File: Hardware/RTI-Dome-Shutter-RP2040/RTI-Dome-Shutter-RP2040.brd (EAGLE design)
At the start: 111.1 x 76.3 mm, 107 parts, among them IC2 24LC64T-I/SN, IC3 FT232RL, IC4 RASPBERRY_PI_PICO, IC8 REG1117-3.3V, IC9 REG1117-5V, J2 XT60PW-M, U1 W5500, X13 PN61729-S, X9 J1011F21PNL

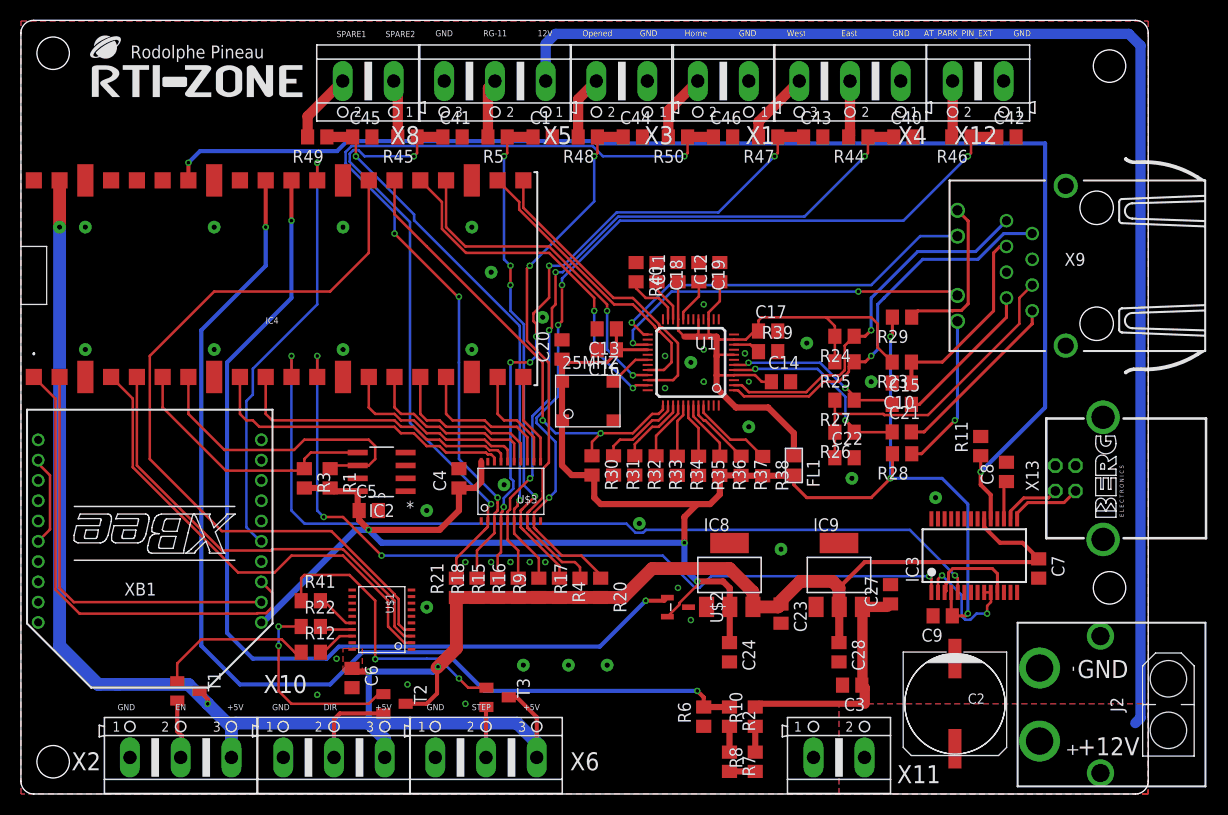
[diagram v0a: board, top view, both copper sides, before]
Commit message: New RP2040 shutter board
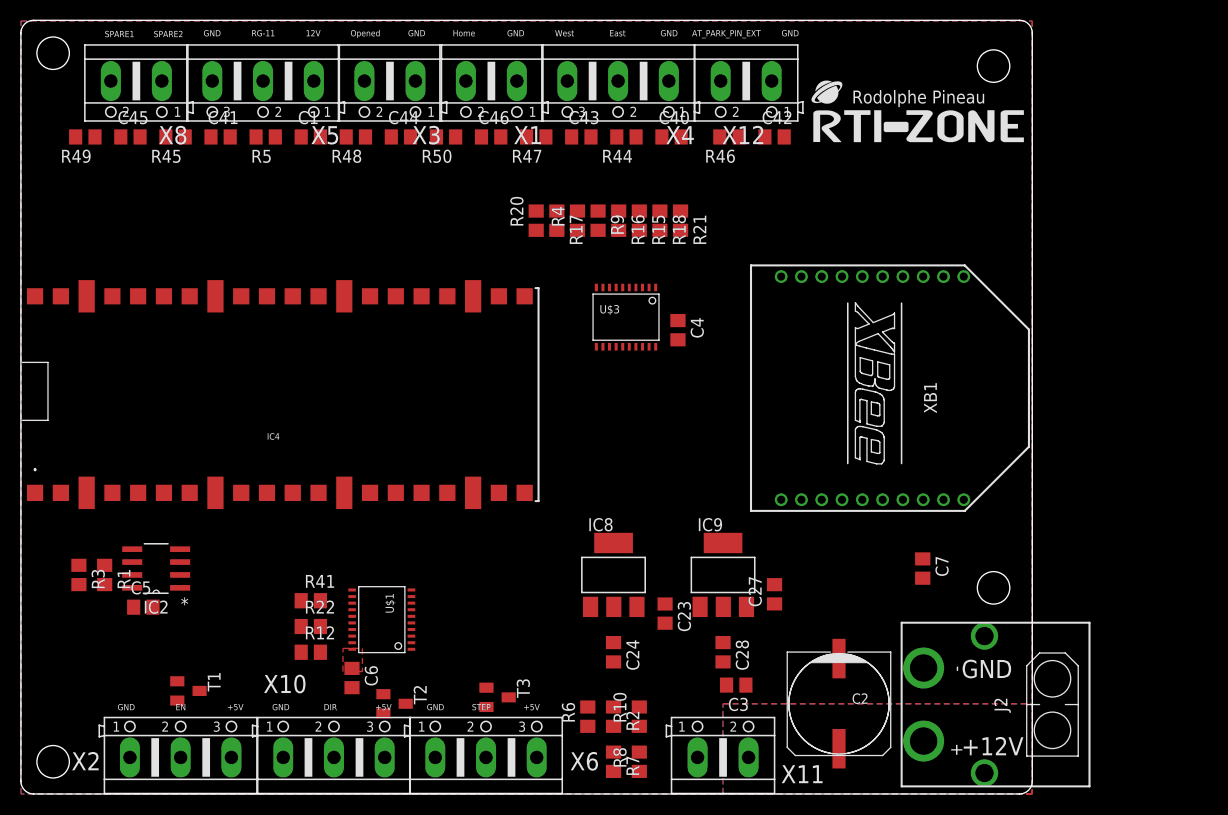
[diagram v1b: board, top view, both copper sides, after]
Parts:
- removed 25MHZ: CB3LV-OSCILATOR, rti:SMD-7050_4P
- removed C10: 22nF, rcl:C0805
- removed C11, C12, C14, C16, C17, C20, C8, C9: 100nF, rcl:C0805
- removed C13, C18, C22: 10nF, rcl:C0805
- removed C15, C21: 6.8nF, rcl:C0805
- removed C19: 4.7uF, rcl:C0805
- removed FL1: BLM21AG121SN1D, BLM21AG121SN1D:L0805
- removed IC3: FT232RL, ftdichip:SSOP28
- removed R11: 10K, rcl:R0805
- removed R23: 10 1%, rcl:R0805
- removed R24, R25, R26, R27: 49.9 1%, rcl:R0805
- removed R28, R29: 330, rcl:R0805
- removed R30, R31, R32, R33, R34, R35, R36, R37, R38, R40: 4.7K, rcl:R0805
- removed R39: 12.4K 1%, rcl:R0805
- removed U$2: MCP120T, MCP120T:SOT95P237X112-3N
- removed U1: W5500, W5500:LQFP48
- removed X13: PN61729-S, rti:PN61729-S
- removed X9: J1011F21PNL, rti:J1011F21PNL
- moved XB1 72.6 mm to (83.9, 40.0), turned to 270 degrees
- moved U$4 71.3 mm to (78.1, 64.3)
- moved R21 42.4 mm to (65.0, 56.5), turned to 270 degrees
- moved R18 40.4 mm to (63.0, 56.5), turned to 270 degrees
- moved R15 38.8 mm to (61.0, 56.5), turned to 270 degrees
- moved R16 37.5 mm to (58.9, 56.5), turned to 270 degrees
- moved R20 36.7 mm to (50.8, 56.5), turned to 90 degrees
- moved R9 36.7 mm to (56.9, 56.5), turned to 270 degrees
- moved R17 36.3 mm to (52.8, 56.5), turned to 270 degrees
- moved R4 36.2 mm to (54.9, 56.5), turned to 90 degrees
- moved C4 26.1 mm to (64.8, 45.7), turned to 270 degrees
- moved C5 24.2 mm to (12.1, 18.4)
- moved IC2 24.2 mm to (13.3, 22.2)
- moved R1 24.2 mm to (8.26, 21.6)
- moved R3 24.2 mm to (5.71, 21.6)
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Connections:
- removed net ACT_LED: U1.27, X9.11
- removed net AVDD: C11.1, C12.1, C14.1, C17.1, FL1.1, R23.2, R24.2, R25.2, U1.11, U1.15, U1.17, U1.21, U1.4, U1.8
- removed net DTR_DSR_DCD: IC3.10, IC3.2, IC3.9
- removed net INT_N: U1.36
- removed net LINK_ACK: U1.25, X9.10
- removed net N$10: R28.1, X9.12
- removed net N$11: C15.2, X9.7
- removed net N$12: C21.2, X9.8
- removed net N$13: C10.1, R23.1, X9.3
- removed net N$17: U1.26
- removed net N$22: R31.1, U1.38
- removed net N$23: R32.1, U1.39
- removed net N$24: R33.1, U1.40
- removed net N$25: R34.1, U1.41
- removed net N$26: R35.1, U1.42
- removed net N$27: R36.1, U1.43
- removed net N$28: R37.1, U1.44
- removed net N$29: R38.1, U1.45
- removed net N$31: C19.2, U1.20
- removed net N$32: U1.18
- removed net N$33: C18.2, U1.22
- removed net N$34: R39.1, U1.10
- removed net N$35: R40.2, U1.23
- removed net N$6: C8.1, IC3.17
- removed net N$7: C22.1, R26.2, R27.2, X9.6
- removed net N$8: R29.1, X9.9
- removed net RTS_CTS: IC3.11, IC3.3
- removed net RXN: C21.1, R26.1, U1.5
- removed net RXP: C15.1, R27.1, U1.6
- removed net TXN: R25.1, U1.1, X9.2
- removed net TXP: R24.1, U1.2, X9.1
- removed net USBD_N: IC3.16, X13.2
- removed net USBD_P: IC3.15, X13.3
- removed net USB_VCC: X13.1
- removed net XI: 25MHZ.3, U1.30
- removed net XO: U1.31
- net 3.3V: no longer 25MHZ.1, 25MHZ.4, C13.1, C16.1, C20.1, C9.1, FL1.2, IC3.4, R28.2, R29.2, R30.2, R36.2, R37.2, R38.2, U$2.2, U1.28
- net ETH_CS: no longer U1.32
- net ETH_RESET: no longer R30.1, U1.37
- net FTDI_RESET: no longer IC3.19, R11.1
- net GND: no longer 25MHZ.2, C10.2, C11.2, C12.2, C13.2, C14.2, C16.2, C17.2, C18.1, C19.1, C20.2, C22.2, C8.2, C9.2, IC3.18, IC3.21, IC3.25, IC3.7, R11.2, R31.2, R32.2, R33.2, R34.2, R35.2, R39.2, R40.1, U$2.3, U1.14, U1.16, U1.19, U1.29, U1.3, U1.48, U1.9, X13.4, X13.S1, X13.S2, X9.4, X9.5, X9.M1, X9.M2
- net RESET: no longer U$2.1
- net RX2: no longer IC3.1
- net SCLK: no longer U1.33
- net SDI: no longer U1.34
- net SDO: no longer U1.35
- net TX2: no longer IC3.5
- net VCC: no longer IC3.20
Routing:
- net VCC: track 219.2 -> 0.00 mm, vias 4 -> 0
- net 3.3V: track 197.7 -> 0.00 mm, vias 6 -> 0
- net +12V: track 154.1 -> 0.00 mm
- net FTDI_RESET: track 128.8 -> 0.00 mm, vias 2 -> 0
- net VPIN: track 106.3 -> 0.00 mm, vias 2 -> 0
- net RESET: track 94.2 -> 0.00 mm, vias 2 -> 0
- net HOME_SHUTTER_CLOSED_IN_5V: track 87.8 -> 0.00 mm, vias 4 -> 0
- net TX2: track 87.4 -> 0.00 mm, vias 2 -> 0
- net AT_PARK_PIN_IN_5V: track 86.0 -> 0.00 mm, vias 4 -> 0
- net RX2: track 82.9 -> 0.00 mm, vias 4 -> 0
- net M_STEP: track 77.4 -> 0.00 mm
- net BUTTON_EAST_OPEN_5V: track 72.4 -> 0.00 mm, vias 4 -> 0
- net AVDD: track 67.6 -> 0.00 mm
- net BUTTON_WEST_CLOSE_IN_5V: track 65.8 -> 0.00 mm, vias 6 -> 0
- net SPARE1_IN_5V: track 60.8 -> 0.00 mm, vias 2 -> 0
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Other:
- board size 111.1 x 76.3 mm -> 99.7 x 76.3 mm
- board text added: "Dome Shutter"
- board text removed: "Dome Rotator / RoR"

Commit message: Switching to 0603 for resistor and capacitors
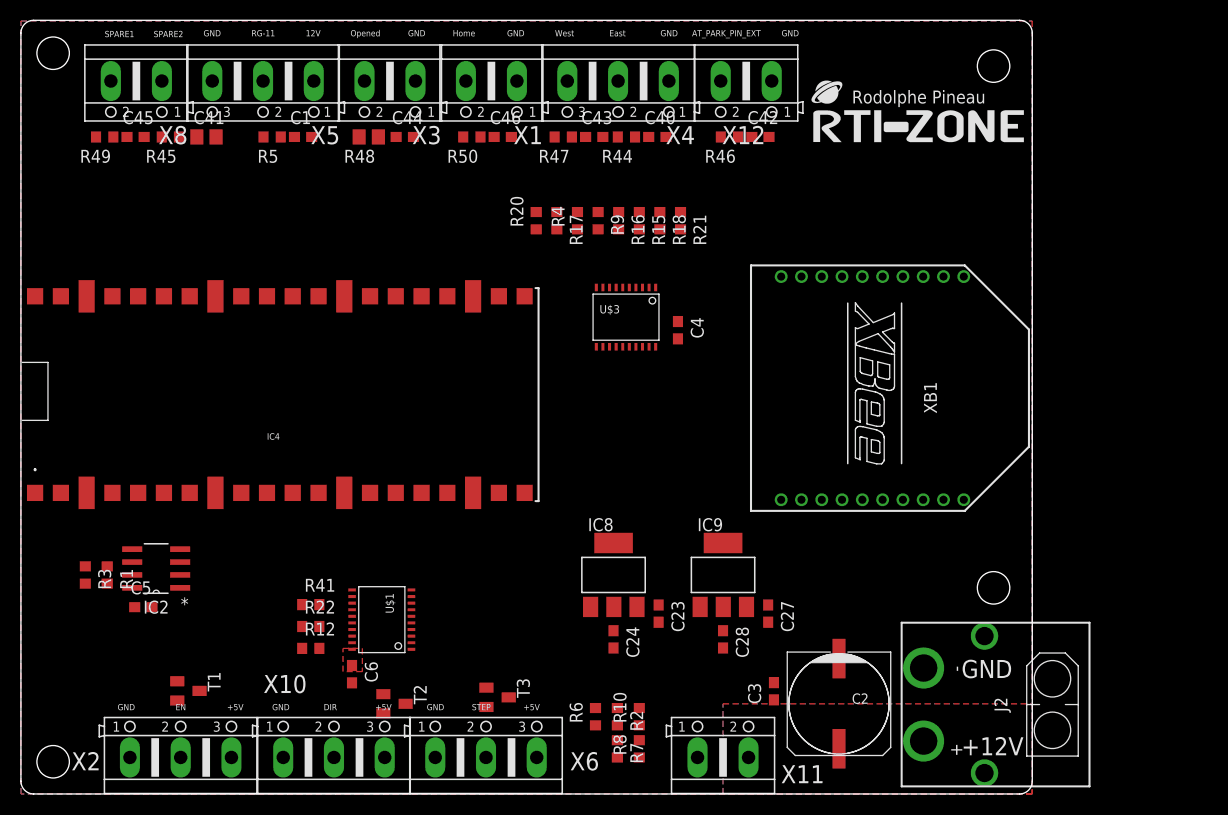
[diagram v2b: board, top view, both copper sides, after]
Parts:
- removed C7: 100nF, rcl:C0805
- C1, C23, C24, C27, C28, C3, C4, C40, C42, C43, C44, C45, C46, C5, C6: device rcl:C0805 -> rcl:C0603
- R1, R10, R12, R15, R16, R17, R18, R2, R20, R21, R22, R3, R4, R41, R44, R45, R46, R47, R49, R5, R50, R6, R7, R8, R9: device rcl:R0805 -> rcl:R0603
- moved C3 3.76 mm to (74.2, 10.1), turned to 90 degrees
- moved R47 2.67 mm to (53.5, 64.8)
- moved R50 2.54 mm to (44.5, 64.8)
- moved C27 2.01 mm to (73.7, 17.8), turned to 270 degrees
- moved R49 1.91 mm to (8.26, 64.8)
- moved C40 1.40 mm to (62.7, 64.8)
- moved C42 1.40 mm to (72.9, 64.8)
- moved C41 1.40 mm to (18.3, 64.8)
- moved R7 1.33 mm to (58.8, 4.45)
- moved C43 1.27 mm to (56.5, 64.8)
- moved R8 1.27 mm to (61.0, 4.45)
- moved C24 1.27 mm to (58.4, 15.2)
- moved C28 1.27 mm to (69.2, 15.2)
- moved R48 1.27 mm to (34.3, 64.8)
- moved C46 1.14 mm to (47.5, 64.8)
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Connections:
- net GND: no longer C7.2
- net VCC: no longer C7.1

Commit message: Routed RP2040 Shutter board
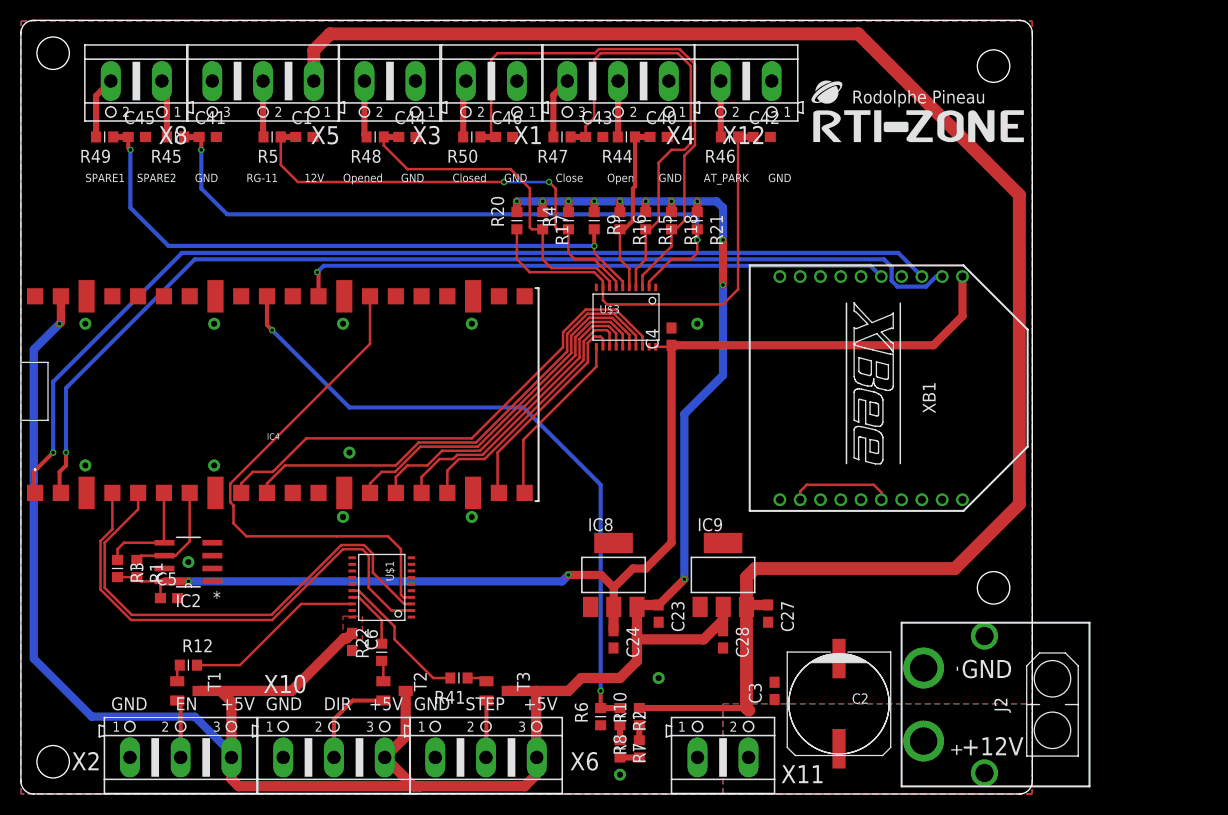
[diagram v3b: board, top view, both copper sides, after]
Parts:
- C1, C23, C24, C27, C28, C3, C4, C40, C42, C43, C44, C45, C46, C5, C6: device rcl:C0603 -> rti:C0603
- C41: device rcl:C0805 -> rti:C0603
- IC2: device Microchip_By_element14_Batch_1:SOIC127P600X175-8N -> rti:SOIC127P600X175-8N
- R1, R10, R12, R15, R16, R17, R18, R2, R20, R21, R22, R3, R4, R41, R44, R45, R46, R47, R49, R5, R50, R6, R7, R8, R9: device rcl:R0603 -> rti:R0603
- R48: device rcl:R0805 -> rti:R0603
- moved R41 16.3 mm to (43.2, 11.4), turned to 180 degrees
- moved R12 12.2 mm to (16.5, 12.7)
- moved R22 7.43 mm to (35.6, 14.0), turned to 90 degrees
- moved R3 3.24 mm to (9.53, 22.2)
- moved IC2 3.24 mm to (16.5, 22.9)
- moved C6 3.18 mm to (32.6, 15.0)
- moved U$1 3.18 mm to (35.6, 20.3)
- moved R1 2.99 mm to (11.4, 22.2)
- moved C5 2.69 mm to (14.6, 19.3)
- moved R20 1.90 mm to (48.9, 56.5)
- moved R21 1.65 mm to (66.7, 56.5)
- moved R17 1.40 mm to (51.4, 56.5)
- moved T2 1.27 mm to (36.8, 10.2)
- moved R18 1.14 mm to (64.1, 56.5)
- moved C4 0.90 mm to (64.1, 45.1), turned to 90 degrees
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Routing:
- net VCC: track 0.00 -> 243.3 mm, vias 0 -> 12
- net +12V: track 0.00 -> 166.2 mm
- net 3.3V: track 0.00 -> 118.3 mm, vias 0 -> 2
- net XBEE_DOUT: track 0.00 -> 104.6 mm, vias 0 -> 1
- net XBEE_DIN: track 0.00 -> 103.7 mm, vias 0 -> 1
- net SPARE1_IN_5V: track 0.00 -> 67.9 mm, vias 0 -> 2
- net VPIN: track 0.00 -> 66.2 mm, vias 0 -> 2
- net SPARE2_IN_5V: track 0.00 -> 62.8 mm, vias 0 -> 2
- net XBEE_RESET: track 0.00 -> 58.7 mm, vias 0 -> 1
- net HOME_SHUTTER_CLOSED_IN_5V: track 0.00 -> 54.8 mm
- net M_STEP: track 0.00 -> 51.4 mm
- net SPARE1: track 0.00 -> 50.6 mm
- net M_EN: track 0.00 -> 49.2 mm
- net M_DIR: track 0.00 -> 48.4 mm
- net HOME_SHUTTER_CLOSED: track 0.00 -> 47.2 mm
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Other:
- board text added: "AT_PARK"
- board text added: "Close"
- board text added: "Closed"
- board text added: "Open"
- board text removed: "AT_PARK_PIN_EXT"
- board text removed: "East"
- board text removed: "Home"
- board text removed: "West"
